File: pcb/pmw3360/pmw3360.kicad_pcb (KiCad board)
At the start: 2 copper layers, 22 x 30 mm, 20 parts, among them J1 Connector, J2 PinOut, U1 PMW3360DM-T2QU, U2 TCR2EF19,LM(CT, U3 SN74LVC1T45QDCKRQ1, U4 TXB0104RUT

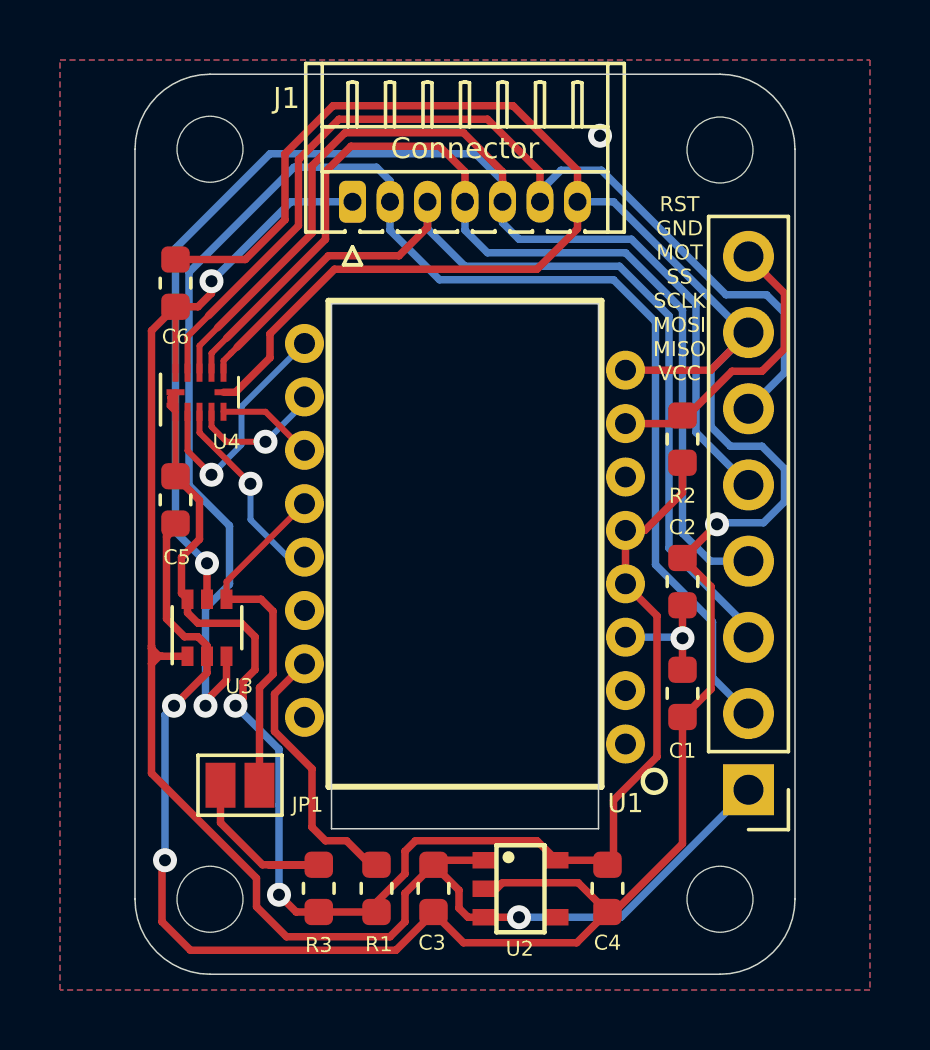
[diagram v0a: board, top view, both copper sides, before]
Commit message: add via
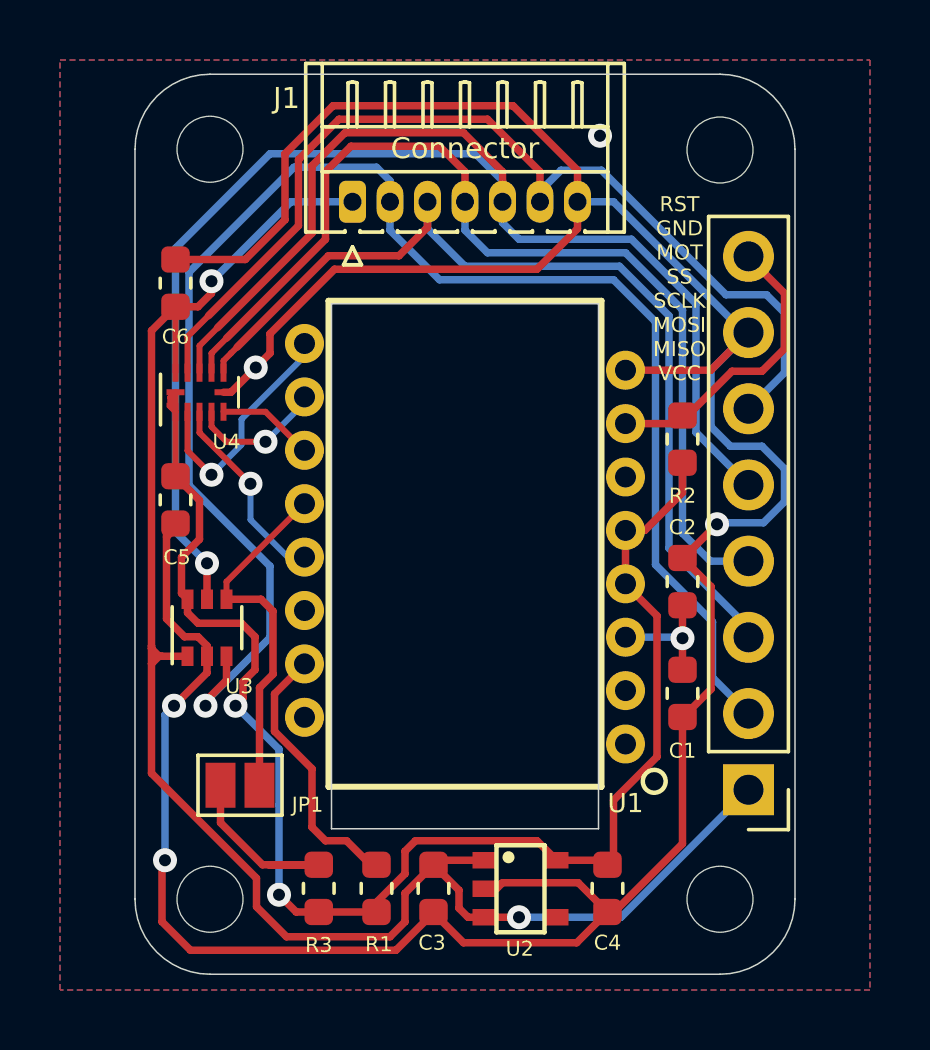
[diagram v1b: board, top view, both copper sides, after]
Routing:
- net /MISO-H: track 51.7 -> 52.8 mm
- net GND: track 108.5 -> 108.4 mm, vias 4 -> 5
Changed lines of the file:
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@@
     (thickness 1.6)
     (drawings 24)
-    (tracks 288)
+    (tracks 291)
     (zones 0)
     (modules 20)
@@
   (segment (start 107.55 106.625) (end 107.75 106.425) (width 0.25) (layer F.Cu) (net 1))
   (segment (start 105.45 107.4) (end 105.45 107.425) (width 0.25) (layer F.Cu) (net 1))
-  (segment (start 110.25 84.625) (end 110.25 83.725) (width 0.25) (layer F.Cu) (net 1))
-  (segment (start 108.9 85.975) (end 110.25 84.625) (width 0.25) (layer F.Cu) (net 1))
-  (segment (start 102.15 85.975) (end 108.9 85.975) (width 0.25) (layer F.Cu) (net 1))
-  (segment (start 98.85 90.075) (end 100 88.925) (width 0.25) (layer F.Cu) (net 1))
-  (segment (start 98.45 90.075) (end 98.85 90.075) (width 0.25) (layer F.Cu) (net 1))
-  (segment (start 100 88.925) (end 100 88.125) (width 0.25) (layer F.Cu) (net 1))
-  (segment (start 100 88.125) (end 102.15 85.975) (width 0.25) (layer F.Cu) (net 1))
   (segment (start 115.81 88.085) (end 115.95 88.085) (width 0.25) (layer B.Cu) (net 1))
   (segment (start 110.25 83.725) (end 111.45 83.725) (width 0.25) (layer B.Cu) (net 1))
@@
   (segment (start 105.45 107.425) (end 106.45 108.425) (width 0.25) (layer F.Cu) (net 1))
   (segment (start 110.225 108.425) (end 111.25 107.4) (width 0.25) (layer F.Cu) (net 1))
+  (segment (start 110.25 84.625) (end 110.25 83.725) (width 0.25) (layer F.Cu) (net 1))
+  (segment (start 98.7 90.075) (end 99.525 89.25) (width 0.25) (layer F.Cu) (net 1))
+  (segment (start 98.45 90.075) (end 98.7 90.075) (width 0.25) (layer F.Cu) (net 1))
+  (segment (start 108.9 85.975) (end 110.25 84.625) (width 0.25) (layer F.Cu) (net 1))
+  (segment (start 100 88.125) (end 102.15 85.975) (width 0.25) (layer F.Cu) (net 1))
+  (segment (start 100 88.775) (end 100 88.125) (width 0.25) (layer F.Cu) (net 1))
+  (segment (start 102.15 85.975) (end 108.9 85.975) (width 0.25) (layer F.Cu) (net 1))
+  (segment (start 99.525 89.25) (end 100 88.775) (width 0.25) (layer F.Cu) (net 1))
+  (via (at 99.525 89.25) (size 0.8) (drill 0.4) (layers F.Cu B.Cu) (net 1))
   (segment (start 111.85 98.24) (end 111.85 98.275) (width 0.25) (layer F.Cu) (net 2))
   (via (at 113.75 98.275) (size 0.8) (drill 0.4) (layers F.Cu B.Cu) (net 2))
@@
   (via (at 97.85 100.525) (size 0.8) (drill 0.4) (layers F.Cu B.Cu) (net 9))
   (segment (start 97.85 100.525) (end 97.85 100.375) (width 0.25) (layer F.Cu) (net 9))
+  (segment (start 104 83.025) (end 104 83.725) (width 0.25) (layer B.Cu) (net 9))
+  (segment (start 100.8 82.575) (end 103.55 82.575) (width 0.25) (layer B.Cu) (net 9))
+  (segment (start 97.3 86.075) (end 100.8 82.575) (width 0.25) (layer B.Cu) (net 9))
   (segment (start 103.55 82.575) (end 104 83.025) (width 0.25) (layer B.Cu) (net 9))
-  (segment (start 100.8 82.575) (end 103.55 82.575) (width 0.25) (layer B.Cu) (net 9))
-  (segment (start 104 83.025) (end 104 83.725) (width 0.25) (layer B.Cu) (net 9))
-  (segment (start 97.3 86.075) (end 100.8 82.575) (width 0.25) (layer B.Cu) (net 9))
-  (segment (start 97.85 97.275) (end 98.65 96.475) (width 0.25) (layer B.Cu) (net 9))
-  (segment (start 97.85 100.525) (end 97.85 97.275) (width 0.25) (layer B.Cu) (net 9))
-  (segment (start 98.65 96.475) (end 98.65 94.525) (width 0.25) (layer B.Cu) (net 9))
-  (segment (start 98.65 94.525) (end 97.3 93.175) (width 0.25) (layer B.Cu) (net 9))
+  (segment (start 97.85 100.525) (end 97.85 100.4) (width 0.25) (layer B.Cu) (net 9))
+  (segment (start 97.85 100.4) (end 100 98.25) (width 0.25) (layer B.Cu) (net 9))
+  (segment (start 100 95.875) (end 97.3 93.175) (width 0.25) (layer B.Cu) (net 9))
   (segment (start 97.3 93.175) (end 97.3 86.075) (width 0.25) (layer B.Cu) (net 9))
+  (segment (start 100 98.25) (end 100 95.875) (width 0.25) (layer B.Cu) (net 9))
   (segment (start 115.95 85.545) (end 115.95 85.575) (width 0.25) (layer F.Cu) (net 10))
   (segment (start 115.95 85.575) (end 117.15 86.775) (width 0.25) (layer F.Cu) (net 10))
@@
   (segment (start 97.25 90.725) (end 97.25 92.025) (width 0.2) (layer F.Cu) (net 17))
   (segment (start 97.25 92.025) (end 98.05 92.825) (width 0.2) (layer F.Cu) (net 17))
+  (segment (start 101.15 88.875) (end 101.15 88.45) (width 0.2) (layer B.Cu) (net 17))
+  (segment (start 99.05 90.975) (end 101.15 88.875) (width 0.2) (layer B.Cu) (net 17))
   (segment (start 98.05 92.825) (end 99.05 91.825) (width 0.2) (layer B.Cu) (net 17))
-  (segment (start 99.05 90.55) (end 101.15 88.45) (width 0.2) (layer B.Cu) (net 17))
-  (segment (start 99.05 91.825) (end 99.05 90.55) (width 0.2) (layer B.Cu) (net 17))
+  (segment (start 99.05 91.825) (end 99.05 90.975) (width 0.2) (layer B.Cu) (net 17))
   (zone (net 1) (net_name GND) (layer F.Cu) (hatch edge 0.508)
     (connect_pads (clearance 0.508))

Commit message: change route
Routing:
- net Net-(JP1-Pad2): track 6.78 -> 4.93 mm
- net GND: track 108.4 -> 106.8 mm
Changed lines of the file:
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@@
     (thickness 1.6)
     (drawings 24)
-    (tracks 291)
+    (tracks 299)
     (zones 0)
     (modules 20)
@@
   (segment (start 113.75 105.125) (end 113.75 100.9) (width 0.25) (layer F.Cu) (net 1))
   (segment (start 111.475 107.4) (end 113.75 105.125) (width 0.25) (layer F.Cu) (net 1))
-  (segment (start 105.45 107.425) (end 104.2 108.675) (width 0.25) (layer F.Cu) (net 1))
-  (segment (start 104.2 108.675) (end 97.35 108.675) (width 0.25) (layer F.Cu) (net 1))
-  (segment (start 97.35 108.675) (end 96.4 107.725) (width 0.25) (layer F.Cu) (net 1))
-  (via (at 96.5 105.675) (size 0.8) (drill 0.4) (layers F.Cu B.Cu) (net 1))
-  (segment (start 96.4 107.725) (end 96.4 105.775) (width 0.25) (layer F.Cu) (net 1))
-  (segment (start 96.4 105.775) (end 96.5 105.675) (width 0.25) (layer F.Cu) (net 1))
   (via (at 96.8 100.525) (size 0.8) (drill 0.4) (layers F.Cu B.Cu) (net 1))
-  (segment (start 96.5 105.675) (end 96.5 100.825) (width 0.25) (layer B.Cu) (net 1))
-  (segment (start 96.5 100.825) (end 96.8 100.525) (width 0.25) (layer B.Cu) (net 1))
   (segment (start 97.9 99.425) (end 97.9 98.875) (width 0.25) (layer F.Cu) (net 1))
   (segment (start 96.8 100.525) (end 97.9 99.425) (width 0.25) (layer F.Cu) (net 1))
@@
   (segment (start 99.525 89.25) (end 100 88.775) (width 0.25) (layer F.Cu) (net 1))
   (via (at 99.525 89.25) (size 0.8) (drill 0.4) (layers F.Cu B.Cu) (net 1))
+  (segment (start 104.2 108.675) (end 105.45 107.425) (width 0.25) (layer F.Cu) (net 1))
+  (segment (start 100.2 107.075) (end 100.2 108.025) (width 0.25) (layer F.Cu) (net 1))
+  (segment (start 98.4 105.275) (end 100.2 107.075) (width 0.25) (layer F.Cu) (net 1))
+  (segment (start 97.5 105.275) (end 98.4 105.275) (width 0.25) (layer F.Cu) (net 1))
+  (segment (start 100.2 108.025) (end 100.85 108.675) (width 0.25) (layer F.Cu) (net 1))
+  (segment (start 96.95 104.725) (end 96.5 104.275) (width 0.25) (layer B.Cu) (net 1))
+  (via (at 96.95 104.725) (size 0.8) (drill 0.4) (layers F.Cu B.Cu) (net 1))
+  (segment (start 96.5 104.275) (end 96.5 100.825) (width 0.25) (layer B.Cu) (net 1))
+  (segment (start 100.85 108.675) (end 104.2 108.675) (width 0.25) (layer F.Cu) (net 1))
+  (segment (start 96.5 100.825) (end 96.8 100.525) (width 0.25) (layer B.Cu) (net 1))
+  (segment (start 96.95 104.725) (end 97.5 105.275) (width 0.25) (layer F.Cu) (net 1))
   (segment (start 111.85 98.24) (end 111.85 98.275) (width 0.25) (layer F.Cu) (net 2))
   (via (at 113.75 98.275) (size 0.8) (drill 0.4) (layers F.Cu B.Cu) (net 2))
@@
   (segment (start 98.05 86.375) (end 100.7 83.725) (width 0.25) (layer B.Cu) (net 3))
   (segment (start 97.6 87.225) (end 96.85 87.225) (width 0.25) (layer F.Cu) (net 3))
+  (segment (start 104.5 106.775) (end 105.45 105.825) (width 0.25) (layer F.Cu) (net 3))
   (segment (start 104.5 107.725) (end 104.5 106.775) (width 0.25) (layer F.Cu) (net 3))
-  (segment (start 96.05 102.775) (end 99.55 106.275) (width 0.25) (layer F.Cu) (net 3))
+  (segment (start 104 108.225) (end 104.5 107.725) (width 0.25) (layer F.Cu) (net 3))
+  (segment (start 96.05 102.775) (end 97.85 104.575) (width 0.25) (layer F.Cu) (net 3))
+  (segment (start 100.75 107.875) (end 101.1 108.225) (width 0.25) (layer F.Cu) (net 3))
   (segment (start 96.05 99.125) (end 96.05 102.775) (width 0.25) (layer F.Cu) (net 3))
-  (segment (start 99.55 106.275) (end 99.55 107.225) (width 0.25) (layer F.Cu) (net 3))
-  (segment (start 104.5 106.775) (end 105.45 105.825) (width 0.25) (layer F.Cu) (net 3))
-  (segment (start 100.55 108.225) (end 104 108.225) (width 0.25) (layer F.Cu) (net 3))
-  (segment (start 104 108.225) (end 104.5 107.725) (width 0.25) (layer F.Cu) (net 3))
-  (segment (start 99.55 107.225) (end 100.55 108.225) (width 0.25) (layer F.Cu) (net 3))
+  (segment (start 97.85 104.575) (end 98.4 104.575) (width 0.25) (layer F.Cu) (net 3))
+  (segment (start 101.1 108.225) (end 104 108.225) (width 0.25) (layer F.Cu) (net 3))
+  (segment (start 98.4 104.575) (end 100.75 106.925) (width 0.25) (layer F.Cu) (net 3))
+  (segment (start 100.75 106.925) (end 100.75 107.875) (width 0.25) (layer F.Cu) (net 3))
   (segment (start 111.85 94.68) (end 111.85 96.46) (width 0.25) (layer F.Cu) (net 4))
   (segment (start 111.85 94.68) (end 111.995 94.68) (width 0.25) (layer F.Cu) (net 4))
@@
   (segment (start 97.25 96.975) (end 97.05 96.775) (width 0.25) (layer F.Cu) (net 4))
   (segment (start 97.05 96.775) (end 97.05 95.575) (width 0.25) (layer F.Cu) (net 4))
-  (via (at 100.3 106.825) (size 0.8) (drill 0.4) (layers F.Cu B.Cu) (net 4))
-  (segment (start 101.625 107.4) (end 100.875 107.4) (width 0.25) (layer F.Cu) (net 4))
-  (segment (start 100.875 107.4) (end 100.3 106.825) (width 0.25) (layer F.Cu) (net 4))
-  (segment (start 100.3 106.825) (end 100.3 103.825) (width 0.25) (layer B.Cu) (net 4))
   (via (at 98.85 100.525) (size 0.8) (drill 0.4) (layers F.Cu B.Cu) (net 4))
-  (segment (start 100.3 103.825) (end 100.3 101.975) (width 0.25) (layer B.Cu) (net 4))
-  (segment (start 100.3 101.975) (end 98.85 100.525) (width 0.25) (layer B.Cu) (net 4))
   (segment (start 97.25 97.425) (end 97.25 96.975) (width 0.25) (layer F.Cu) (net 4))
   (segment (start 97.6 97.775) (end 97.25 97.425) (width 0.25) (layer F.Cu) (net 4))
@@
   (segment (start 112.9 102.225) (end 111.45 103.675) (width 0.25) (layer F.Cu) (net 4))
   (segment (start 111.45 103.675) (end 111.45 105.625) (width 0.25) (layer F.Cu) (net 4))
+  (segment (start 101.45 103.125) (end 98.85 100.525) (width 0.25) (layer B.Cu) (net 4))
+  (segment (start 101.45 103.475) (end 101.45 103.125) (width 0.25) (layer B.Cu) (net 4))
+  (segment (start 100.5 104.425) (end 101.45 103.475) (width 0.25) (layer B.Cu) (net 4))
+  (via (at 100.5 105.475) (size 0.8) (drill 0.4) (layers F.Cu B.Cu) (net 4))
+  (segment (start 100.5 105.475) (end 100.5 104.425) (width 0.25) (layer B.Cu) (net 4))
+  (segment (start 101.625 107.1) (end 101.625 107.4) (width 0.25) (layer F.Cu) (net 4))
+  (segment (start 100.5 105.475) (end 100.5 105.975) (width 0.25) (layer F.Cu) (net 4))
+  (segment (start 100.5 105.975) (end 101.625 107.1) (width 0.25) (layer F.Cu) (net 4))
   (segment (start 109 83.725) (end 109 84.275) (width 0.25) (layer B.Cu) (net 5))
   (segment (start 97.25 89.425) (end 97.25 88.225) (width 0.2) (layer F.Cu) (net 5))
@@
   (segment (start 98.55 96.975) (end 99.7 96.975) (width 0.25) (layer F.Cu) (net 11))
   (segment (start 99.7 96.975) (end 100.1 97.375) (width 0.25) (layer F.Cu) (net 11))
-  (segment (start 99.95 105.825) (end 101.625 105.825) (width 0.25) (layer F.Cu) (net 12))
-  (segment (start 98.35 103.175) (end 98.35 104.425) (width 0.25) (layer F.Cu) (net 12))
-  (segment (start 99.75 105.825) (end 101.625 105.825) (width 0.25) (layer F.Cu) (net 12))
-  (segment (start 98.35 104.425) (end 99.75 105.825) (width 0.25) (layer F.Cu) (net 12))
+  (segment (start 98.35 103.85) (end 98.35 103.175) (width 0.25) (layer F.Cu) (net 12))
+  (segment (start 98.925 104.425) (end 98.35 103.85) (width 0.25) (layer F.Cu) (net 12))
+  (segment (start 100.5 104.425) (end 98.925 104.425) (width 0.25) (layer F.Cu) (net 12))
+  (segment (start 101.625 105.825) (end 101.625 105.55) (width 0.25) (layer F.Cu) (net 12))
+  (segment (start 101.625 105.55) (end 100.5 104.425) (width 0.25) (layer F.Cu) (net 12))
   (segment (start 100.15 100.13) (end 101.15 99.13) (width 0.25) (layer F.Cu) (net 13))
   (segment (start 101.4 102.625) (end 100.15 101.375) (width 0.25) (layer F.Cu) (net 13))

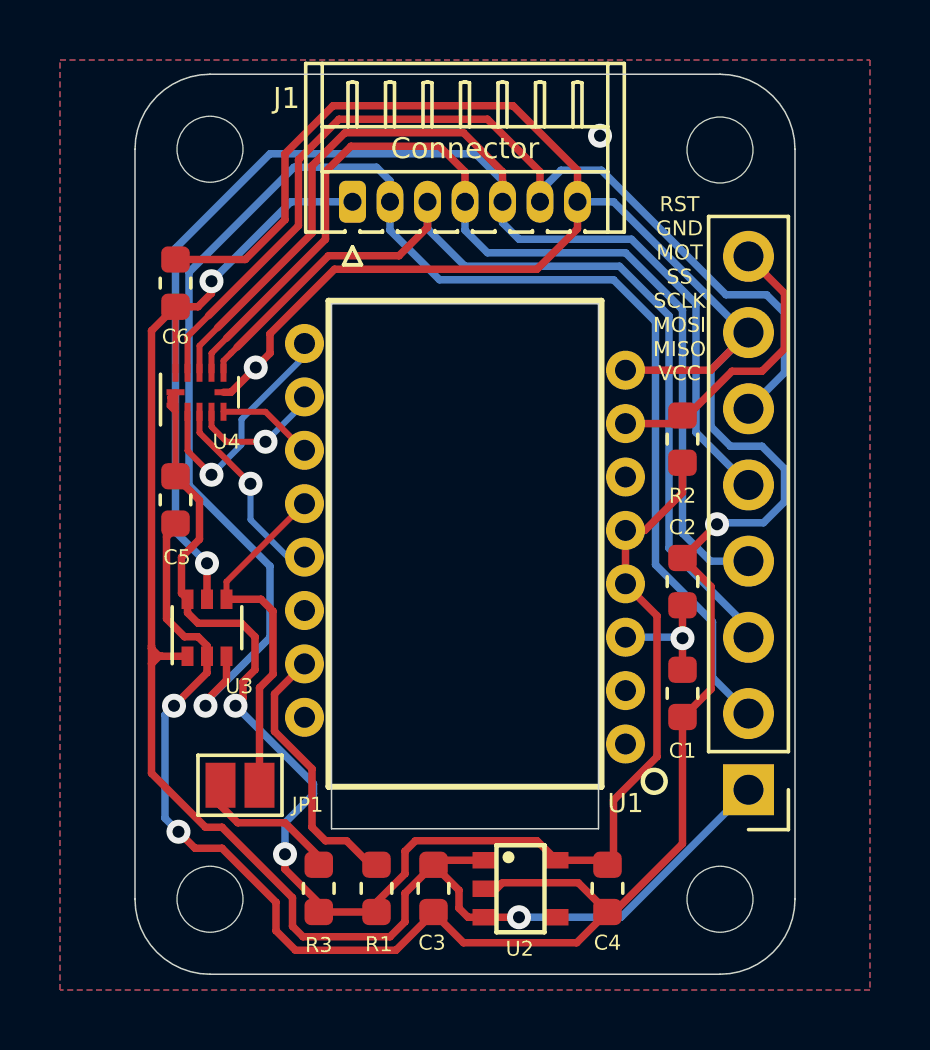
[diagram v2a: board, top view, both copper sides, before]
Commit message: change route
avoid mounting hole
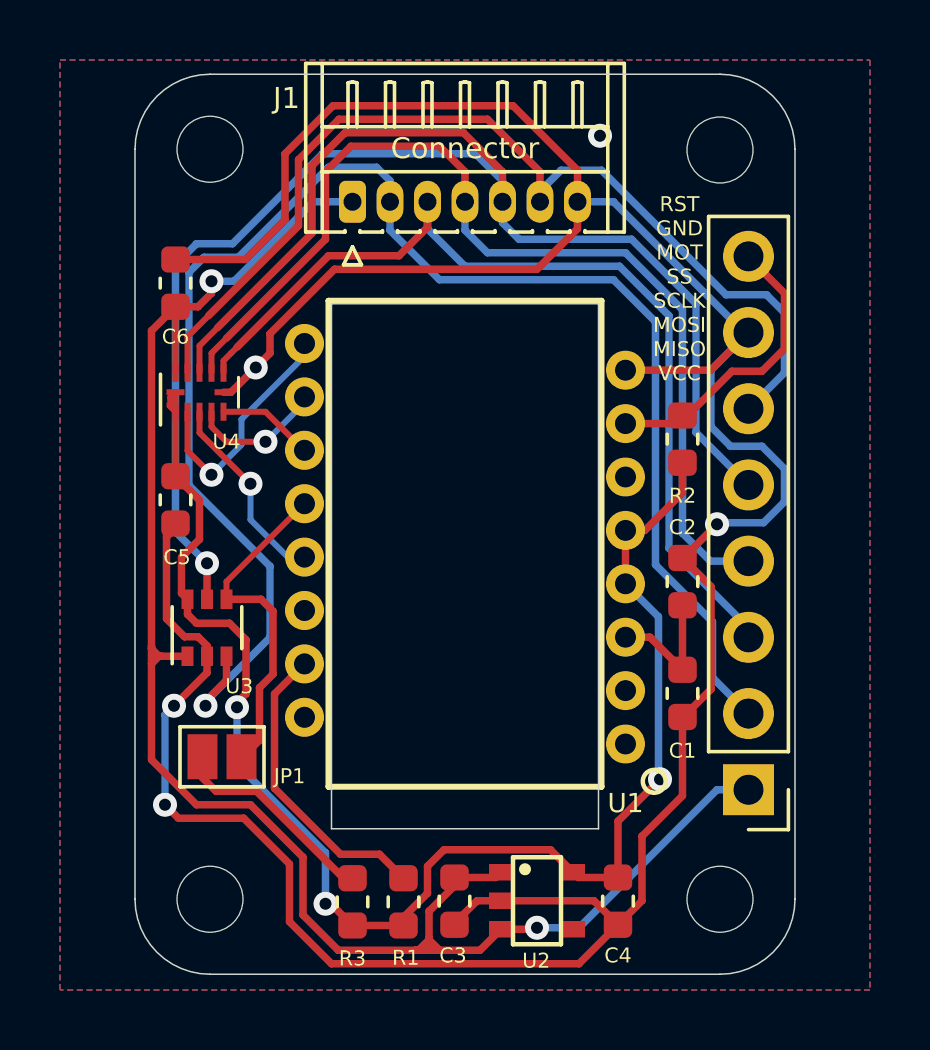
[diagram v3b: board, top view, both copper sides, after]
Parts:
- moved R3 1.21 mm to (102.8, 107.1)
- moved JP1 1.12 mm to (98.4, 102.2)
- moved R1 1.01 mm to (104.5, 107.1)
- moved C3 0.82 mm to (106.2, 107.0)
- moved U2 0.68 mm to (108.9, 107.0)
- moved C4 0.55 mm to (111.6, 107.0)
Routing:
- net VCC: track 56.3 -> 58.7 mm
- net Net-(JP1-Pad2): track 4.93 -> 7.09 mm
- net GND: track 106.8 -> 108.5 mm
- net Net-(R1-Pad1): track 9.04 -> 10.1 mm
- net /MISO: track 12.0 -> 11.3 mm
- net VDD: track 50.3 -> 49.8 mm, vias 2 -> 3
- net Net-(C1-Pad1): track 4.10 -> 4.53 mm, vias 1 -> 0
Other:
- board text added: "Cut out here"
